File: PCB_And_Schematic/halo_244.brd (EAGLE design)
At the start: 88.9 x 49.2 mm, 12 parts

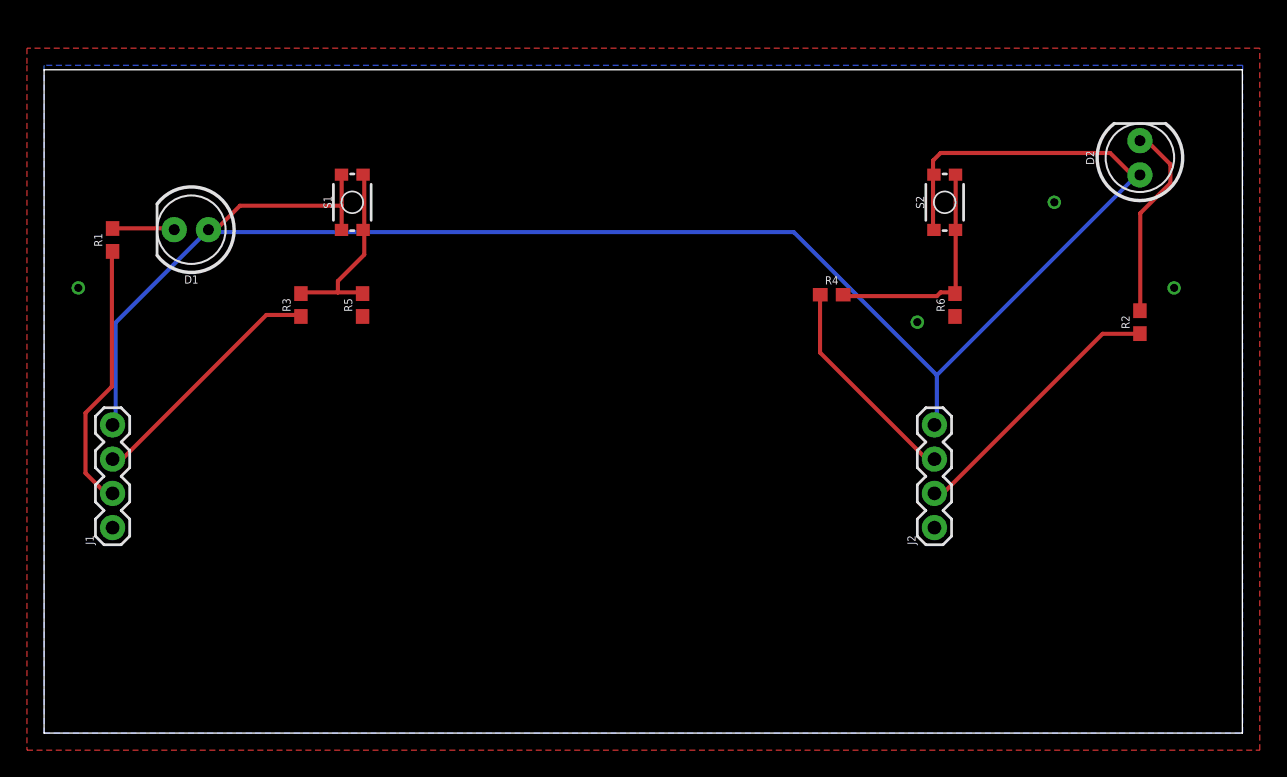
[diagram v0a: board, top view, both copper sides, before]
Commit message: reduced the size of board
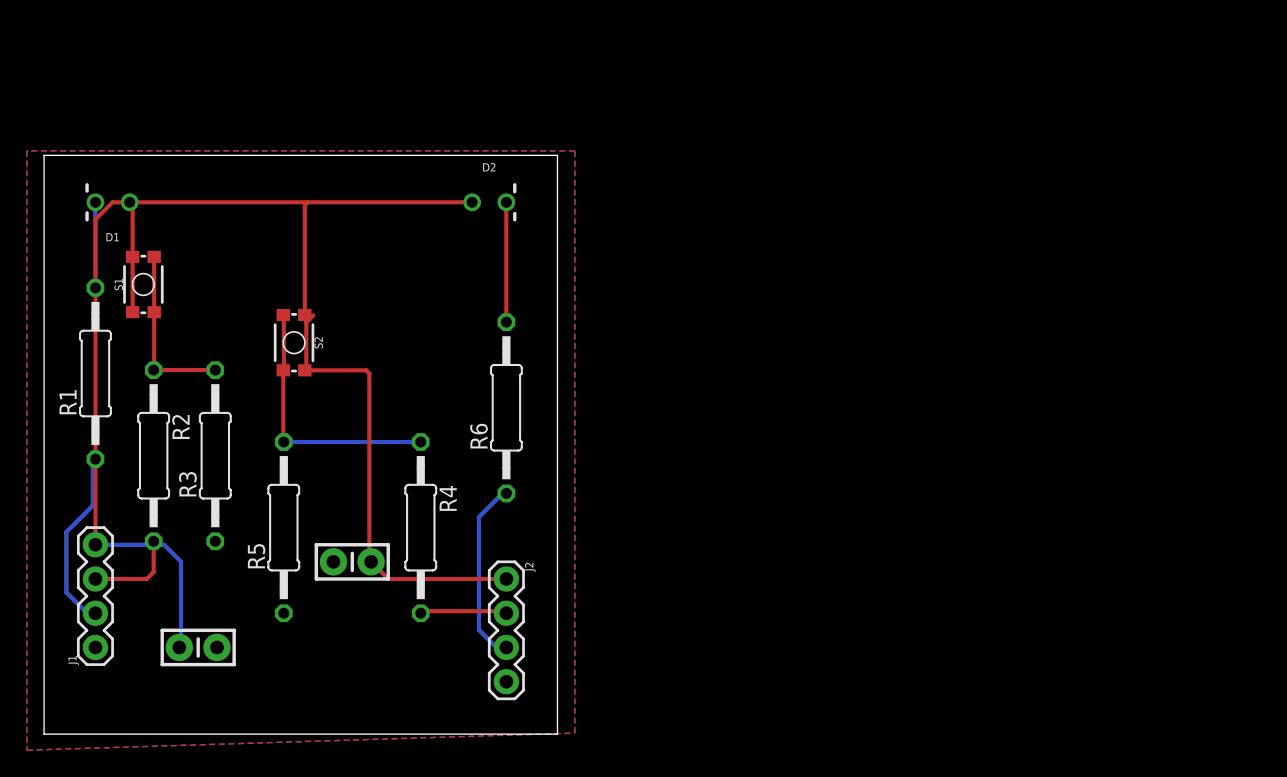
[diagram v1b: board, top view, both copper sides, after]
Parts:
- added C1, C2: 0.1uF, SparkFun-Capacitors:CAP-PTH-SMALL-KIT
- D1, D2: value red -> (none); device SparkFun-LED:LED_5MM -> SparkFun-LED:LED_3MM-NS
- R1: value 4.7k -> 470; device SparkFun-Resistors:0603 -> rcl:0207/12
- R2: value 4.7k -> 1k; device SparkFun-Resistors:0603 -> rcl:0207/12
- R3: value 1k -> 10k; device SparkFun-Resistors:0603 -> rcl:0207/12
- R4, R5: device SparkFun-Resistors:0603 -> rcl:0207/12
- R6: value 10k -> 470; device SparkFun-Resistors:0603 -> rcl:0207/12
- moved R2 73.8 mm to (8.13, 20.6), turned to 270 degrees
- moved S2 49.4 mm to (18.5, 29.0), turned to 270 degrees
- moved D2 48.4 mm to (33.0, 39.4), turned to 0 degrees
- moved R4 35.0 mm to (27.9, 15.2), turned to 270 degrees
- moved R6 34.1 mm to (34.3, 24.1)
- moved J2 32.0 mm to (34.3, 11.4), turned to 270 degrees
- moved R5 17.5 mm to (17.8, 15.2)
- moved S1 16.7 mm to (7.37, 33.3)
- moved R3 12.9 mm to (12.7, 20.6)
- moved R1 9.99 mm to (3.81, 26.7)
- moved J1 8.98 mm to (3.81, 6.35)
- moved D1 6.19 mm to (5.08, 39.4)
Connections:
- net GND: now also C1.2, C2.2, J2.4, R3.1; no longer J2.1, R6.1
- net LED2: now also J2.3, R6.1; no longer J2.2, R2.1
- net N$1: now also R2.1; no longer R5.2
- net N$3: now also R6.2; no longer R2.2
- net N$4: now also R4.1, R5.2; no longer R4.2, R6.2
- net SW1: now also R2.2; no longer R3.1
- net SW2: now also J2.2, R4.2; no longer J2.3, R4.1
- net VCC: now also C1.1, C2.1, J2.1; no longer J2.4
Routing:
- net VCC: track 137.2 -> 120.5 mm
- net SW1: track 18.5 -> 6.81 mm
- net SW2: track 16.0 -> 6.50 mm
- net LED2: track 20.1 -> 13.8 mm
- net LED1: track 19.9 -> 13.6 mm
- net N$3: track 14.8 -> 9.11 mm
- net N$4: track 17.3 -> 19.6 mm
- net N$2: track 4.60 -> 6.56 mm
- net N$1: track 14.3 -> 13.0 mm
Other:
- board size 88.9 x 49.2 mm -> 38.1 x 42.9 mm

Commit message: final pcb files
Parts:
- S1, S2: value (none) -> MOMENTARY-SWITCH-SPST-PTH-6.0MM; device SparkFun-Switches:TACTILE_SWITCH_SMD_4.6X2.8MM -> SparkFun-Switches:TACTILE_SWITCH_PTH_6.0MM
- moved R6 31.7 mm to (58.7, 44.5)
- moved S2 31.6 mm to (47.6, 41.3), turned to 90 degrees
- moved C1 31.2 mm to (50.8, 26.7)
- moved J1 30.5 mm to (16.1, 34.3), turned to 270 degrees
- moved R5 29.3 mm to (38.6, 35.8), turned to 270 degrees
- moved J2 28.8 mm to (58.7, 26.7), turned to 90 degrees
- moved R3 27.1 mm to (35.3, 35.6), turned to 270 degrees
- moved R4 24.2 mm to (47.5, 29.5), turned to 0 degrees
- moved C2 23.4 mm to (23.1, 26.7)
- moved D2 22.1 mm to (55.0, 41.3), turned to 180 degrees
- moved S1 21.7 mm to (27.6, 41.3)
- moved R1 21.6 mm to (16.1, 44.5)
- moved R2 21.0 mm to (25.9, 31.8), turned to 180 degrees
- moved D1 15.5 mm to (20.3, 42.0)
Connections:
- net N$1: no longer S1.2
- net N$4: no longer S2.2
- net VCC: no longer S1.4, S2.4
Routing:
- net VCC: track 120.5 -> 82.9 mm
- net N$1: track 13.0 -> 18.2 mm
- net N$3: track 9.11 -> 14.0 mm
- net N$4: track 19.6 -> 14.8 mm
- net N$2: track 6.56 -> 11.3 mm
- net LED2: track 13.8 -> 10.2 mm
- net LED1: track 13.6 -> 11.0 mm
- net SW2: track 6.50 -> 4.93 mm
- net SW1: track 6.81 -> 5.82 mm
- removed copper zone on layer 16, net GND
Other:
- board size 38.1 x 42.9 mm -> 49 x 28.2 mm
- board text added: "Team: Halo"
